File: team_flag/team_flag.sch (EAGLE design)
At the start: 9 parts, among them Q1 MOSFET-LOGIC-NCHANNELSMD, Q2 MOSFET-LOGIC-NCHANNELSMD

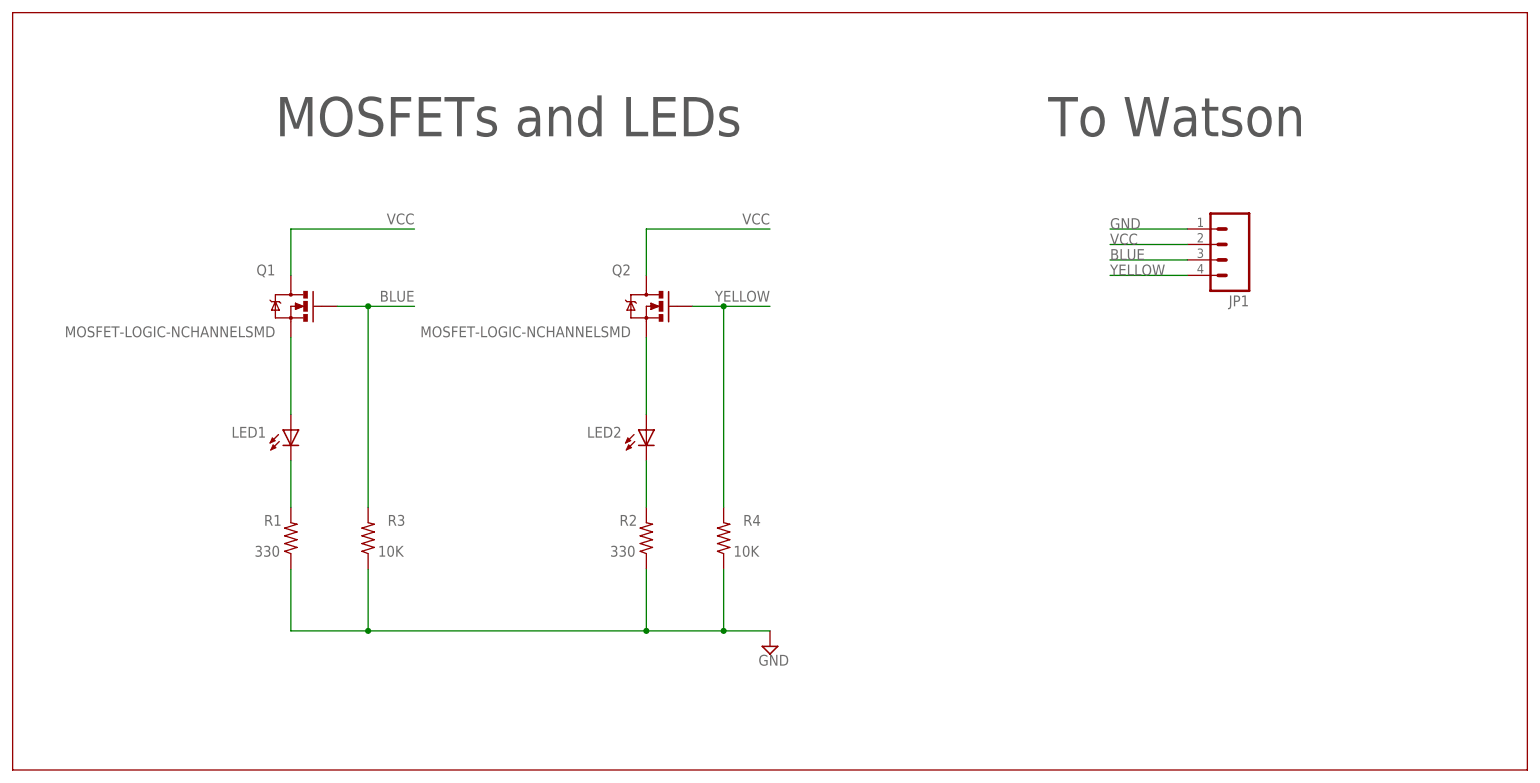
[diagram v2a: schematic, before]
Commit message: Team Flag Rev C
-rearranged circuitry
-Used proper 4-pin MTA footprint
-Moved bPlace signal labels to be more visible
-Replaced 330 Ohm with 200 Ohm resistors
-Updated silkscreen and schematic information
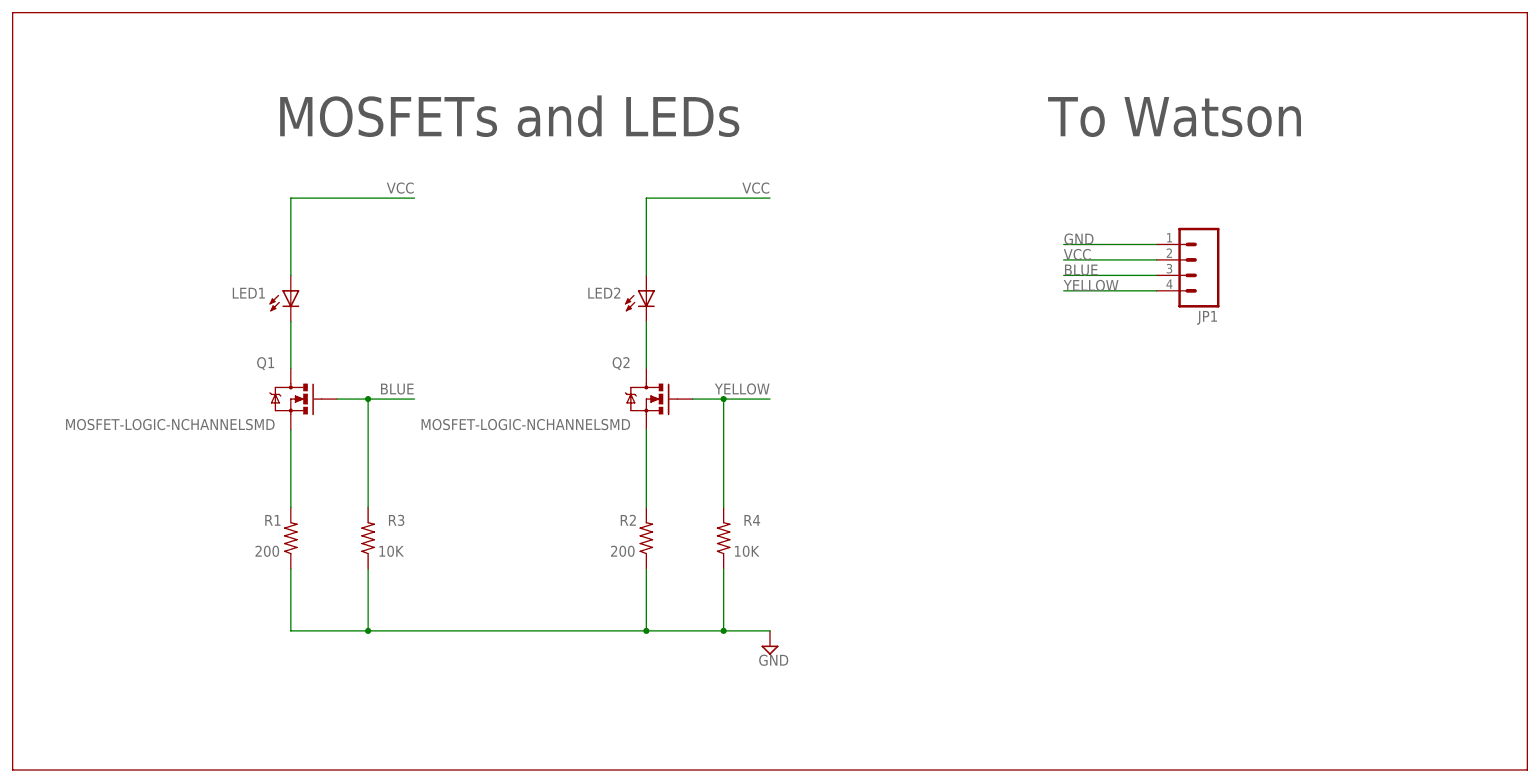
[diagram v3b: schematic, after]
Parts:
- JP1: device pie:M04PTH -> pie:M041X04-MTA
- R1, R2: value 330 -> 200
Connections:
- removed net BSIGNAL: LED1.A, Q1.S
- removed net YSIGNAL: LED2.A, Q2.S
- new net BSOURCE: Q1.S, R1.2
- new net YSOURCE: Q2.S, R2.2
- net BDRAIN: now also Q1.D; no longer R1.2
- net VCC: now also LED1.A, LED2.A; no longer Q1.D, Q2.D
- net YDRAIN: now also Q2.D; no longer R2.2
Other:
- moved on the sheet: JP1, LED1, LED2, Q1, Q2
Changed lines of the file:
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@@
 <part name="LED1" library="led" deviceset="LED" device="5MM"/>
 <part name="LED2" library="led" deviceset="LED" device="5MM"/>
-<part name="R1" library="rcl" deviceset="R-US_" device="R0603" value="330"/>
-<part name="R2" library="rcl" deviceset="R-US_" device="R0603" value="330"/>
+<part name="R1" library="rcl" deviceset="R-US_" device="R0603" value="200"/>
+<part name="R2" library="rcl" deviceset="R-US_" device="R0603" value="200"/>
 <part name="Q1" library="pie" deviceset="MOSFET-LOGIC-NCHANNEL" device="SMD"/>
 <part name="Q2" library="pie" deviceset="MOSFET-LOGIC-NCHANNEL" device="SMD"/>
-<part name="JP1" library="pie" deviceset="M04" device="PTH"/>
 <part name="SUPPLY1" library="pie" deviceset="GND" device=""/>
 <part name="FRAME1" library="pie" deviceset="FRAME-LETTER" device="">
 <attribute name="AUTHOR" value="Aravind K., Jared P."/>
-<attribute name="REVISION" value="B"/>
+<attribute name="REVISION" value="C"/>
 </part>
 <part name="R3" library="rcl" deviceset="R-US_" device="R0603" value="10K"/>
 <part name="R4" library="rcl" deviceset="R-US_" device="R0603" value="10K"/>
+<part name="JP1" library="pie" deviceset="M04" device="1X04-MTA"/>
 </parts>
 <sheets>
@@
 </plain>
 <instances>
-<instance part="LED1" gate="G$1" x="45.72" y="55.88" smashed="yes">
-<attribute name="NAME" x="41.656" y="56.388" size="1.778" layer="95" rot="R180"/>
-<attribute name="VALUE" x="51.435" y="51.308" size="1.778" layer="96" rot="R90"/>
+<instance part="LED1" gate="G$1" x="45.72" y="78.74" smashed="yes">
+<attribute name="NAME" x="41.656" y="79.248" size="1.778" layer="95" rot="R180"/>
+<attribute name="VALUE" x="51.435" y="74.168" size="1.778" layer="96" rot="R90"/>
 </instance>
-<instance part="LED2" gate="G$1" x="104.14" y="55.88" smashed="yes">
-<attribute name="NAME" x="100.076" y="56.388" size="1.778" layer="95" rot="R180"/>
-<attribute name="VALUE" x="109.855" y="51.308" size="1.778" layer="96" rot="R90"/>
+<instance part="LED2" gate="G$1" x="104.14" y="78.74" smashed="yes">
+<attribute name="NAME" x="100.076" y="79.248" size="1.778" layer="95" rot="R180"/>
+<attribute name="VALUE" x="109.855" y="74.168" size="1.778" layer="96" rot="R90"/>
 </instance>
 <instance part="R1" gate="G$1" x="45.72" y="38.1" smashed="yes" rot="R90">
@@
 <attribute name="VALUE" x="102.362" y="36.83" size="1.778" layer="96" rot="R180"/>
 </instance>
-<instance part="Q1" gate="G$1" x="45.72" y="76.2" smashed="yes" rot="MR0">
-<attribute name="NAME" x="43.18" y="81.28" size="1.778" layer="95" rot="MR0"/>
-<attribute name="VALUE" x="43.18" y="71.12" size="1.778" layer="96" rot="MR0"/>
+<instance part="Q1" gate="G$1" x="45.72" y="60.96" smashed="yes" rot="MR0">
+<attribute name="NAME" x="43.18" y="66.04" size="1.778" layer="95" rot="MR0"/>
+<attribute name="VALUE" x="43.18" y="55.88" size="1.778" layer="96" rot="MR0"/>
 </instance>
-<instance part="Q2" gate="G$1" x="104.14" y="76.2" smashed="yes" rot="MR0">
-<attribute name="NAME" x="101.6" y="81.28" size="1.778" layer="95" rot="MR0"/>
-<attribute name="VALUE" x="101.6" y="71.12" size="1.778" layer="96" rot="MR0"/>
+<instance part="Q2" gate="G$1" x="104.14" y="60.96" smashed="yes" rot="MR0">
+<attribute name="NAME" x="101.6" y="66.04" size="1.778" layer="95" rot="MR0"/>
+<attribute name="VALUE" x="101.6" y="55.88" size="1.778" layer="96" rot="MR0"/>
 </instance>
-<instance part="JP1" gate="G$1" x="200.66" y="86.36" rot="R180"/>
 <instance part="SUPPLY1" gate="GND" x="124.46" y="20.32"/>
 <instance part="FRAME1" gate="G$2" x="147.32" y="0">
@@
 <attribute name="VALUE" x="122.682" y="36.83" size="1.778" layer="96" rot="R180"/>
 </instance>
+<instance part="JP1" gate="G$1" x="195.58" y="83.82" rot="R180"/>
 </instances>
 <busses>
@@
 <net name="YELLOW" class="0">
 <segment>
-<pinref part="JP1" gate="G$1" pin="4"/>
-<wire x1="193.04" y1="81.28" x2="180.34" y2="81.28" width="0.1524" layer="91"/>
-<label x="180.34" y="81.28" size="1.778" layer="95"/>
+<pinref part="Q2" gate="G$1" pin="G"/>
+<wire x1="111.76" y1="60.96" x2="116.84" y2="60.96" width="0.1524" layer="91"/>
+<label x="124.46" y="63.5" size="1.778" layer="95" rot="R180"/>
+<junction x="116.84" y="60.96"/>
+<wire x1="116.84" y1="60.96" x2="124.46" y2="60.96" width="0.1524" layer="91"/>
+<pinref part="R4" gate="G$1" pin="2"/>
+<wire x1="116.84" y1="60.96" x2="116.84" y2="43.18" width="0.1524" layer="91"/>
 </segment>
 <segment>
-<pinref part="Q2" gate="G$1" pin="G"/>
-<wire x1="111.76" y1="76.2" x2="116.84" y2="76.2" width="0.1524" layer="91"/>
-<label x="124.46" y="78.74" size="1.778" layer="95" rot="R180"/>
-<junction x="116.84" y="76.2"/>
-<wire x1="116.84" y1="76.2" x2="124.46" y2="76.2" width="0.1524" layer="91"/>
-<pinref part="R4" gate="G$1" pin="2"/>
-<wire x1="116.84" y1="76.2" x2="116.84" y2="43.18" width="0.1524" layer="91"/>
+<pinref part="JP1" gate="G$1" pin="4"/>
+<wire x1="187.96" y1="78.74" x2="172.72" y2="78.74" width="0.1524" layer="91"/>
+<label x="172.72" y="78.74" size="1.778" layer="95"/>
 </segment>
 </net>
 <net name="VCC" class="0">
 <segment>
-<pinref part="JP1" gate="G$1" pin="2"/>
-<wire x1="193.04" y1="86.36" x2="180.34" y2="86.36" width="0.1524" layer="91"/>
-<label x="180.34" y="86.36" size="1.778" layer="95"/>
+<wire x1="104.14" y1="93.98" x2="124.46" y2="93.98" width="0.1524" layer="91"/>
+<label x="124.46" y="96.52" size="1.778" layer="95" rot="R180"/>
+<pinref part="LED2" gate="G$1" pin="A"/>
+<wire x1="104.14" y1="93.98" x2="104.14" y2="81.28" width="0.1524" layer="91"/>
 </segment>
 <segment>
-<pinref part="Q2" gate="G$1" pin="D"/>
-<wire x1="104.14" y1="81.28" x2="104.14" y2="88.9" width="0.1524" layer="91"/>
-<wire x1="104.14" y1="88.9" x2="124.46" y2="88.9" width="0.1524" layer="91"/>
-<label x="124.46" y="91.44" size="1.778" layer="95" rot="R180"/>
+<wire x1="45.72" y1="93.98" x2="66.04" y2="93.98" width="0.1524" layer="91"/>
+<label x="66.04" y="96.52" size="1.778" layer="95" rot="R180"/>
+<pinref part="LED1" gate="G$1" pin="A"/>
+<wire x1="45.72" y1="93.98" x2="45.72" y2="81.28" width="0.1524" layer="91"/>
 </segment>
 <segment>
-<pinref part="Q1" gate="G$1" pin="D"/>
-<wire x1="45.72" y1="88.9" x2="45.72" y2="81.28" width="0.1524" layer="91"/>
-<wire x1="45.72" y1="88.9" x2="66.04" y2="88.9" width="0.1524" layer="91"/>
-<label x="66.04" y="91.44" size="1.778" layer="95" rot="R180"/>
-</segment>
-</net>
-<net name="YSIGNAL" class="0">
-<segment>
-<pinref part="Q2" gate="G$1" pin="S"/>
-<pinref part="LED2" gate="G$1" pin="A"/>
-<wire x1="104.14" y1="71.12" x2="104.14" y2="58.42" width="0.1524" layer="91"/>
-</segment>
-</net>
-<net name="BSIGNAL" class="0">
-<segment>
-<pinref part="LED1" gate="G$1" pin="A"/>
-<pinref part="Q1" gate="G$1" pin="S"/>
-<wire x1="45.72" y1="58.42" x2="45.72" y2="71.12" width="0.1524" layer="91"/>
-</segment>
-</net>
-<net name="BDRAIN" class="0">
-<segment>
-<pinref part="LED1" gate="G$1" pin="C"/>
-<pinref part="R1" gate="G$1" pin="2"/>
-<wire x1="45.72" y1="50.8" x2="45.72" y2="43.18" width="0.1524" layer="91"/>
-</segment>
-</net>
-<net name="YDRAIN" class="0">
-<segment>
-<pinref part="LED2" gate="G$1" pin="C"/>
-<pinref part="R2" gate="G$1" pin="2"/>
-<wire x1="104.14" y1="50.8" x2="104.14" y2="43.18" width="0.1524" layer="91"/>
+<pinref part="JP1" gate="G$1" pin="2"/>
+<wire x1="187.96" y1="83.82" x2="172.72" y2="83.82" width="0.1524" layer="91"/>
+<label x="172.72" y="83.82" size="1.778" layer="95"/>
 </segment>
 </net>
@@
 <segment>
 <pinref part="JP1" gate="G$1" pin="1"/>
-<wire x1="193.04" y1="88.9" x2="180.34" y2="88.9" width="0.1524" layer="91"/>
-<label x="180.34" y="88.9" size="1.778" layer="95"/>
+<wire x1="187.96" y1="86.36" x2="172.72" y2="86.36" width="0.1524" layer="91"/>
+<label x="172.72" y="86.36" size="1.778" layer="95"/>
 </segment>
 </net>
@@
 <segment>
 <pinref part="Q1" gate="G$1" pin="G"/>
-<wire x1="53.34" y1="76.2" x2="58.42" y2="76.2" width="0.1524" layer="91"/>
-<label x="66.04" y="78.74" size="1.778" layer="95" rot="R180"/>
-<wire x1="58.42" y1="76.2" x2="66.04" y2="76.2" width="0.1524" layer="91"/>
-<wire x1="58.42" y1="76.2" x2="58.42" y2="43.18" width="0.1524" layer="91"/>
-<junction x="58.42" y="76.2"/>
+<wire x1="53.34" y1="60.96" x2="58.42" y2="60.96" width="0.1524" layer="91"/>
+<label x="66.04" y="63.5" size="1.778" layer="95" rot="R180"/>
+<wire x1="58.42" y1="60.96" x2="66.04" y2="60.96" width="0.1524" layer="91"/>
+<wire x1="58.42" y1="60.96" x2="58.42" y2="43.18" width="0.1524" layer="91"/>
+<junction x="58.42" y="60.96"/>
 <pinref part="R3" gate="G$1" pin="2"/>
 </segment>
 <segment>
 <pinref part="JP1" gate="G$1" pin="3"/>
-<wire x1="193.04" y1="83.82" x2="180.34" y2="83.82" width="0.1524" layer="91"/>
-<label x="180.34" y="83.82" size="1.778" layer="95"/>
+<wire x1="187.96" y1="81.28" x2="172.72" y2="81.28" width="0.1524" layer="91"/>
+<label x="172.72" y="81.28" size="1.778" layer="95"/>
 </segment>
 </net>
+<net name="BDRAIN" class="0">
+<segment>
+<pinref part="LED1" gate="G$1" pin="C"/>
+<pinref part="Q1" gate="G$1" pin="D"/>
+<wire x1="45.72" y1="73.66" x2="45.72" y2="66.04" width="0.1524" layer="91"/>
+</segment>
+</net>
+<net name="BSOURCE" class="0">
+<segment>
+<pinref part="Q1" gate="G$1" pin="S"/>
+<pinref part="R1" gate="G$1" pin="2"/>
+<wire x1="45.72" y1="55.88" x2="45.72" y2="43.18" width="0.1524" layer="91"/>
+</segment>
+</net>
+<net name="YDRAIN" class="0">
+<segment>
+<pinref part="LED2" gate="G$1" pin="C"/>
+<pinref part="Q2" gate="G$1" pin="D"/>
+<wire x1="104.14" y1="73.66" x2="104.14" y2="66.04" width="0.1524" layer="91"/>
+</segment>
+</net>
+<net name="YSOURCE" class="0">
+<segment>
+<pinref part="Q2" gate="G$1" pin="S"/>
+<pinref part="R2" gate="G$1" pin="2"/>
+<wire x1="104.14" y1="55.88" x2="104.14" y2="43.18" width="0.1524" layer="91"/>
+</segment>
+</net>

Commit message: Team Flag Rev C pt 2
-changed resistors from 200 to 330
-moved 330 resistors to the drain-side of the MOSFETs
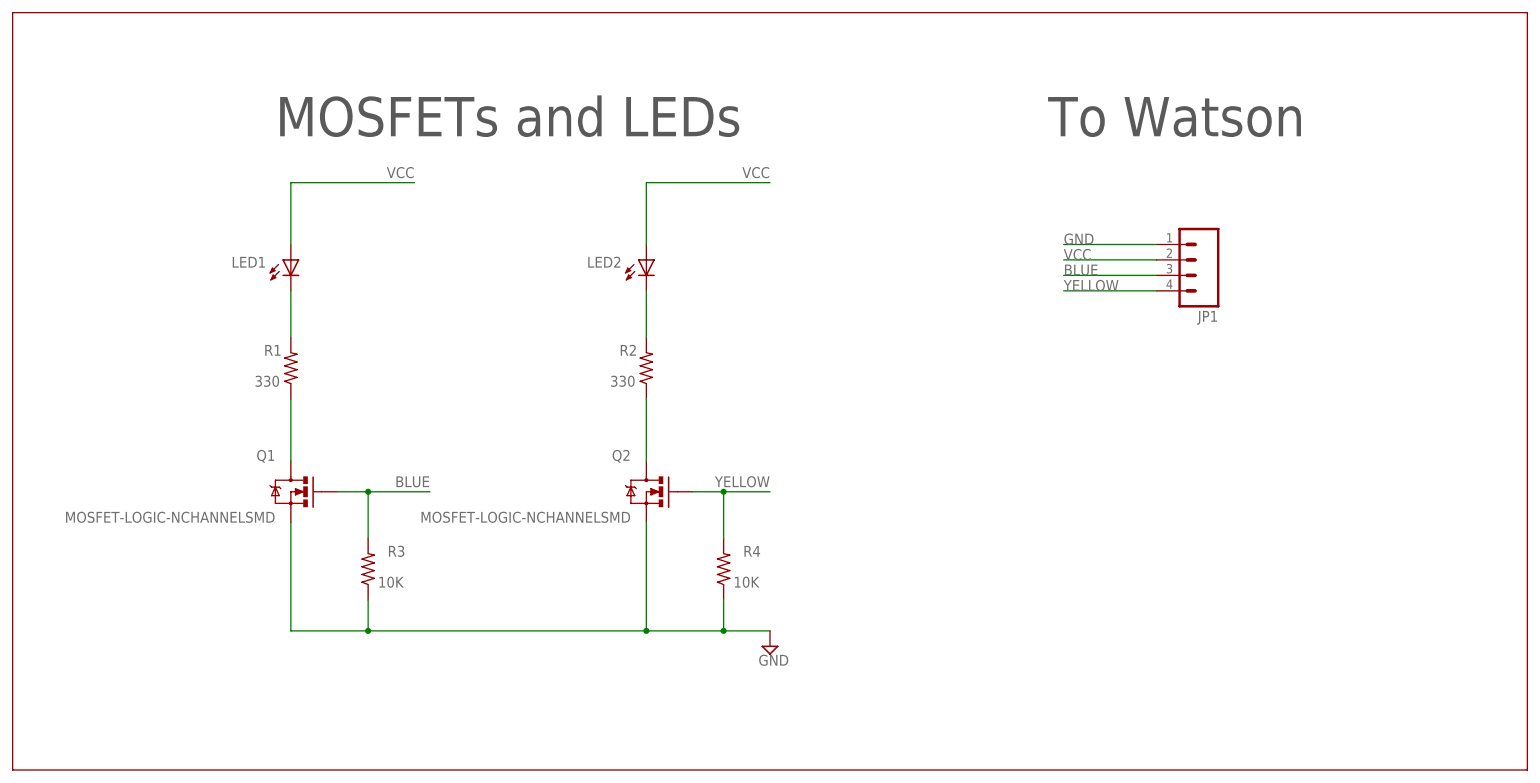
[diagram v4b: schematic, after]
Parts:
- R1, R2: value 200 -> 330
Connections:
- removed net BDRAIN: LED1.C, Q1.D
- removed net YDRAIN: LED2.C, Q2.D
- new net N$2: LED1.C, R1.2
- new net N$3: LED2.C, R2.2
- net BSOURCE: now also Q1.D, R1.1; no longer Q1.S, R1.2
- net GND: now also Q1.S, Q2.S; no longer R1.1, R2.1
- net YSOURCE: now also Q2.D, R2.1; no longer Q2.S, R2.2
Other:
- moved on the sheet: LED1, LED2, Q1, Q2, R1, R2, R3, R4

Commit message: Team Flag Rev C pt 4
-reoriented MTA footprint again
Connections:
- net BLUE: now also JP1.2; no longer JP1.3
- net GND: now also JP1.4; no longer JP1.1
- net VCC: now also JP1.3; no longer JP1.2
- net YELLOW: now also JP1.1; no longer JP1.4
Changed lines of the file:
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@@
 </segment>
 <segment>
-<pinref part="JP1" gate="G$1" pin="4"/>
-<wire x1="187.96" y1="78.74" x2="172.72" y2="78.74" width="0.1524" layer="91"/>
-<label x="172.72" y="78.74" size="1.778" layer="95"/>
+<pinref part="JP1" gate="G$1" pin="1"/>
+<wire x1="187.96" y1="86.36" x2="172.72" y2="86.36" width="0.1524" layer="91"/>
+<label x="172.72" y="86.36" size="1.778" layer="95"/>
 </segment>
 </net>
@@
 </segment>
 <segment>
-<pinref part="JP1" gate="G$1" pin="2"/>
-<wire x1="187.96" y1="83.82" x2="172.72" y2="83.82" width="0.1524" layer="91"/>
-<label x="172.72" y="83.82" size="1.778" layer="95"/>
+<pinref part="JP1" gate="G$1" pin="3"/>
+<wire x1="187.96" y1="81.28" x2="172.72" y2="81.28" width="0.1524" layer="91"/>
+<label x="172.72" y="81.28" size="1.778" layer="95"/>
 </segment>
 </net>
@@
 </segment>
 <segment>
-<pinref part="JP1" gate="G$1" pin="1"/>
-<wire x1="187.96" y1="86.36" x2="172.72" y2="86.36" width="0.1524" layer="91"/>
-<label x="172.72" y="86.36" size="1.778" layer="95"/>
+<pinref part="JP1" gate="G$1" pin="4"/>
+<wire x1="187.96" y1="78.74" x2="172.72" y2="78.74" width="0.1524" layer="91"/>
+<label x="172.72" y="78.74" size="1.778" layer="95"/>
 </segment>
 </net>
@@
 </segment>
 <segment>
-<pinref part="JP1" gate="G$1" pin="3"/>
-<wire x1="187.96" y1="81.28" x2="172.72" y2="81.28" width="0.1524" layer="91"/>
-<label x="172.72" y="81.28" size="1.778" layer="95"/>
+<pinref part="JP1" gate="G$1" pin="2"/>
+<wire x1="187.96" y1="83.82" x2="172.72" y2="83.82" width="0.1524" layer="91"/>
+<label x="172.72" y="83.82" size="1.778" layer="95"/>
 </segment>
 </net>
